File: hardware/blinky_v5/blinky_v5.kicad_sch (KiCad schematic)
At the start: 239 parts, among them J1 RJ45, J10 Conn_01x04, J11 Conn_01x08, J12 Conn_01x06, J2 Conn_01x06_Pin, J3 Conn_01x05_Pin, J5 Conn_01x06_Pin, J6 Conn_01x04_Pin, J7 Conn_01x04_Pin, J8 Conn_01x02, J9 Conn_02x10_Odd_Even, Q1 2N7002, Q10 2N7002, Q2 2N7002, Q3 2N7002, Q4 2N7002, Q5 2N7002, Q6 2N7002, Q7 2N7002, Q8 2N7002, Q9 2N7002, U1 ADA4807-1, U10 STM32F405RGTx, U11 AMS1117-3.3, U12 BA50DD0WHFP-TR, U13 M24C02-RMN, U2 SN74LVC1G14DBV, U3 SN74LVC1G14DBV, U4 ADA4807-1, U5 ADA4807-1, U6 TLV3603DCKR, U7 SN74LVC1G14DBV, U8 TLV3603DCKR, U9 L78L05_SOT89, X1 GTXO-14V (2.048MHz), X2 GTXO-14V (2.048MHz), Y1 AOCJY4A-10.000MHZ-SW, Y2 16MHz

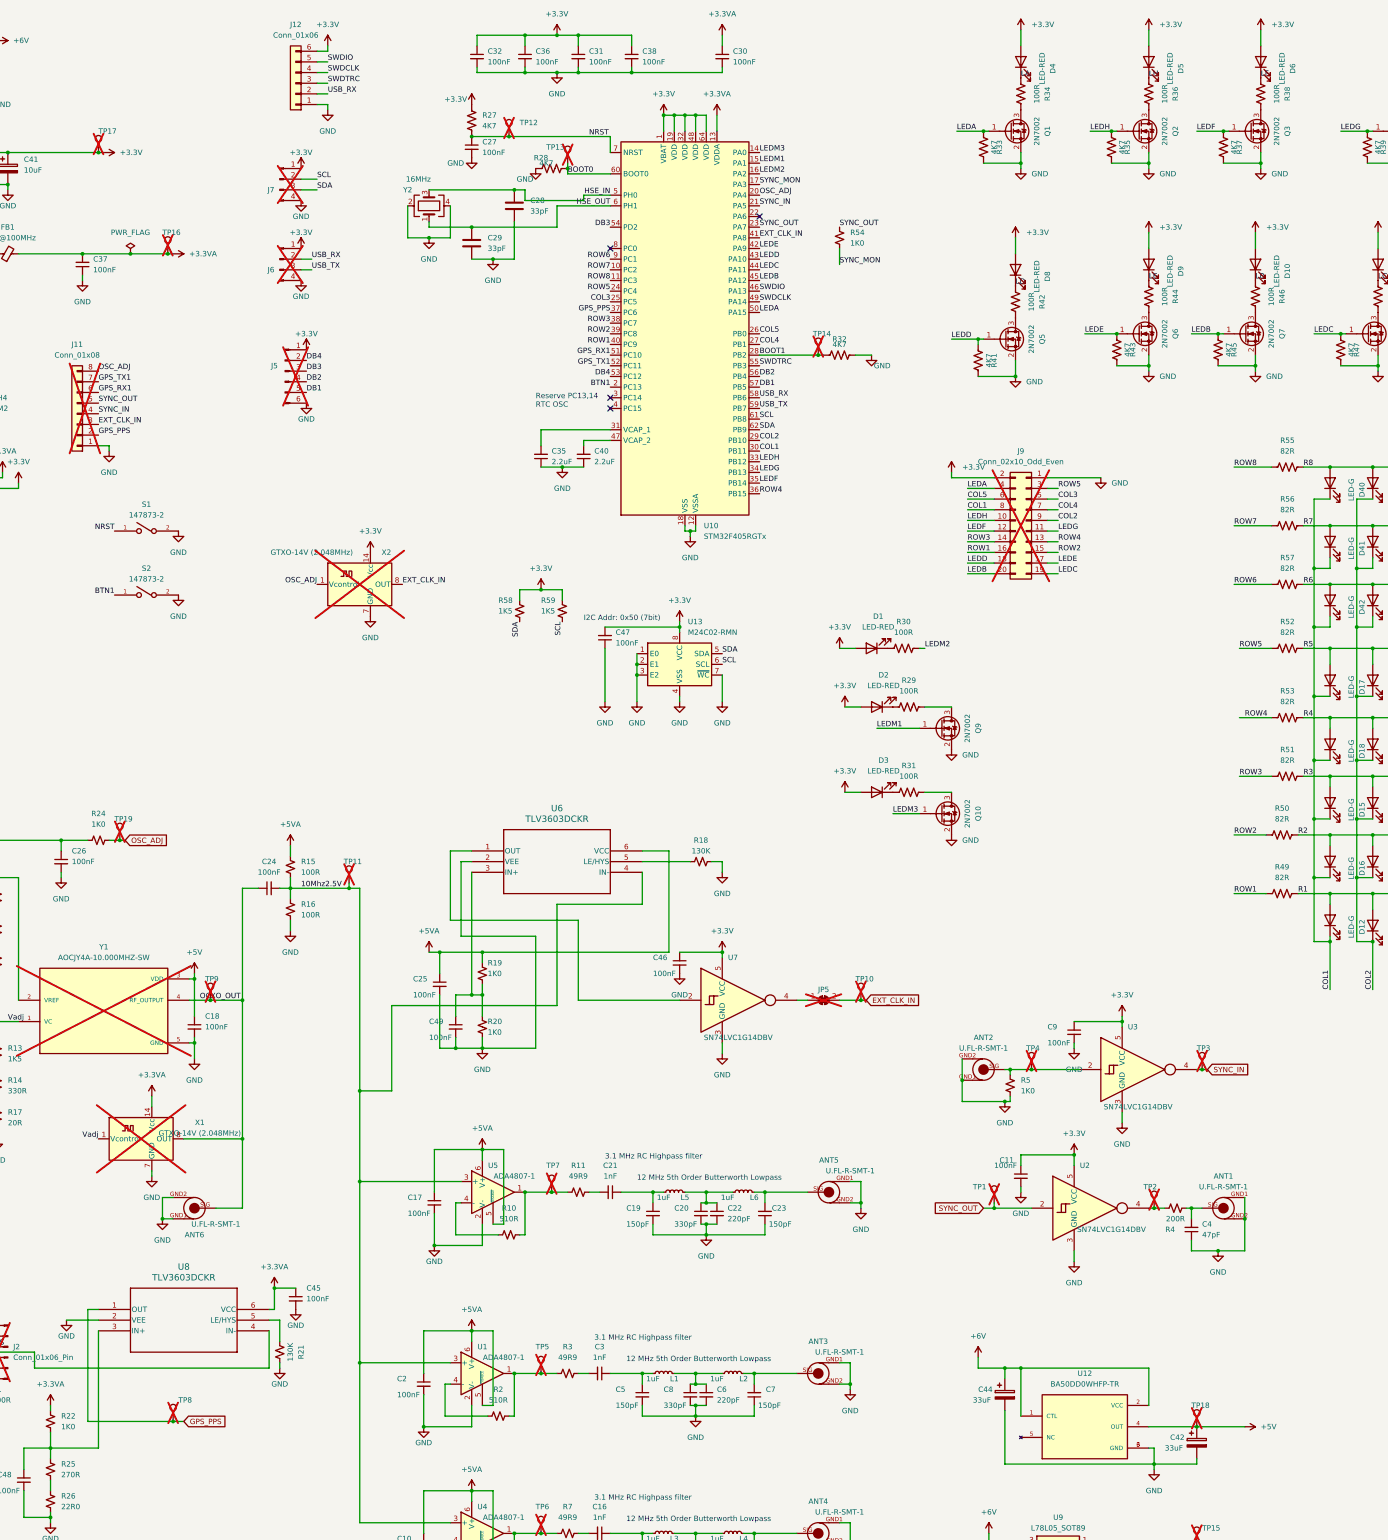
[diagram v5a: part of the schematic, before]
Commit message: update schematic for new pin out
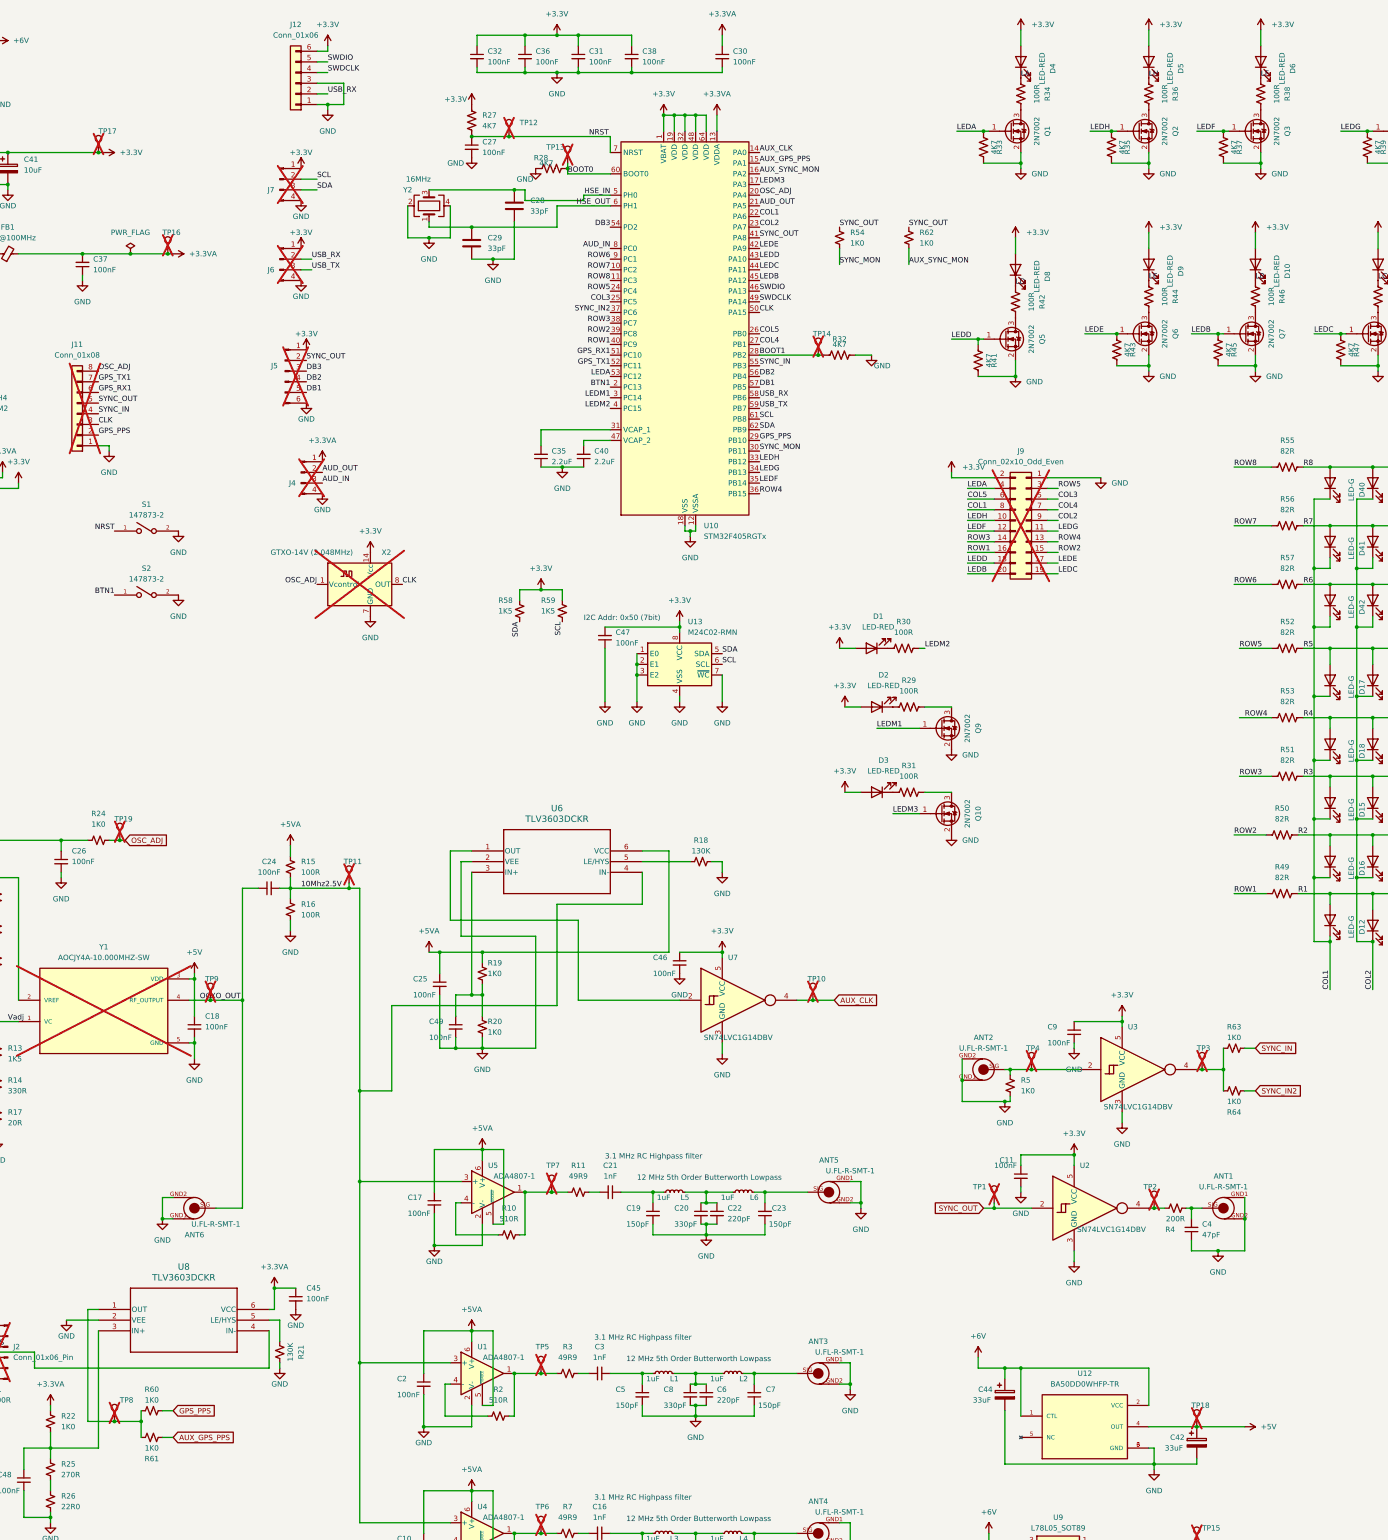
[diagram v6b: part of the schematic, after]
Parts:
- removed JP5: SolderJumper_2_Bridged, Jumper:SolderJumper-2_P1.3mm_Bridged_RoundedPad1.0x1.5mm, symbol Jumper:SolderJumper_2_Bridged
- removed X1: GTXO-14V (2.048MHz), Oscillator:Oscillator_DIP-14, symbol Oscillator:GTXO-14V
- added J4: Conn_01x04_Pin, Connector_PinHeader_2.54mm:PinHeader_1x04_P2.54mm_Vertical, symbol Connector:Conn_01x04_Pin
- added R60, R61, R62, R63, R64: 1K0, Resistor_SMD:R_0603_1608Metric, symbol Device:R_Small_US
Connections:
- net +3.3VA: now also J4.1 (Pin_1)
- net COL1: now also U10.22 (PA6); no longer U10.30 (PB11)
- net COL2: now also U10.23 (PA7); no longer U10.29 (PB10)
- net GND: now also J12.3 (Pin_3), J4.4 (Pin_4)
- net GPS_PPS: now also U10.29 (PB10), R60.1; no longer TP8.1, U10.37 (PC6), U8.1 (OUT)
- net LEDA: now also U10.53 (PC12); no longer U10.50 (PA15)
- net LEDM1: now also U10.3 (PC14); no longer U10.15 (PA1)
- net LEDM2: now also U10.4 (PC15); no longer U10.16 (PA2)
- net LEDM3: now also U10.17 (PA3); no longer U10.14 (PA0)
- net SYNC_IN: now also U10.55 (PB3), R63.1; no longer TP3.1, U10.21 (PA5), U3.4
- net SYNC_MON: now also U10.30 (PB11); no longer U10.17 (PA3)
- net SYNC_OUT: now also J5.2 (Pin_2), U10.41 (PA8), R62.1; no longer U10.23 (PA7)
- net AUX_CLK: now reaches U7.4
- net AUX_CLK: now also TP10.1, U10.14 (PA0)
- net AUD_IN: now reaches U10.8 (PC0)
- net AUD_IN: now also J4.3 (Pin_3)
- removed net DB4: J5.2 (Pin_2), U10.53 (PC12)
- net EXT_CLK_IN renamed CLK
- net CLK: now also U10.50 (PA15); no longer TP10.1, U10.41 (PA8)
- removed net SWDTRC: J12.3 (Pin_3), U10.55 (PB3)
- new net: R60.2, R61.1, TP8.1, U8.1 (OUT)
- new net: R63.2, R64.2, TP3.1, U3.4
- new net AUD_OUT: J4.2 (Pin_2), U10.21 (PA5)
- new net AUX_GPS_PPS: R61.2, U10.15 (PA1)
- new net AUX_SYNC_MON: R62.2, U10.16 (PA2)
- new net SYNC_IN2: R64.1, U10.37 (PC6)
- no-connect marks 4 -> 0
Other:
- note removed: "Reserve PC13,14 RTC OSC"
- moved on the sheet: TP10, TP8

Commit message: update scehmatic with new pin out
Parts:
- removed J10: Conn_01x04, Connector_PinHeader_2.54mm:PinHeader_1x04_P2.54mm_Vertical, symbol Connector_Generic:Conn_01x04
- removed J11: Conn_01x08, Connector_PinHeader_2.54mm:PinHeader_1x08_P2.54mm_Vertical, symbol Connector_Generic:Conn_01x08
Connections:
- net LEDM1: now also U10.4 (PC15); no longer U10.3 (PC14)
- net LEDM2: now also U10.17 (PA3); no longer U10.4 (PC15)
- net LEDM3: now also U10.3 (PC14); no longer U10.17 (PA3)

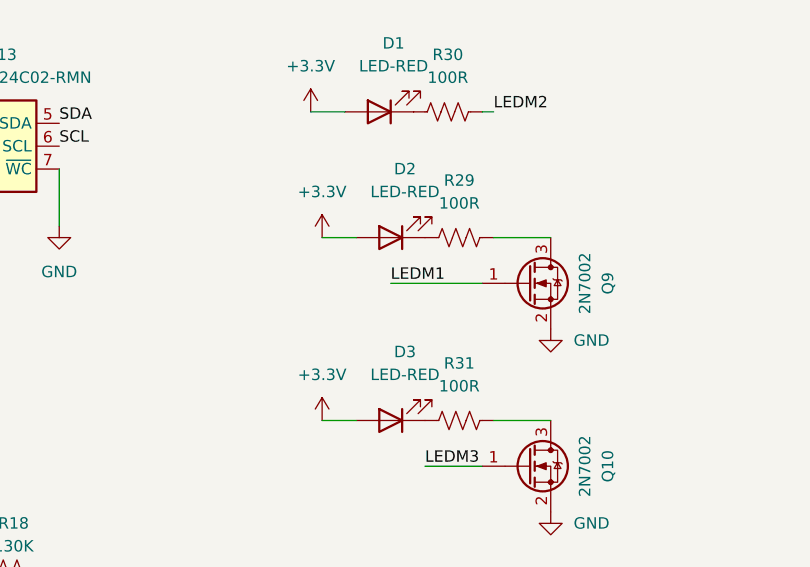
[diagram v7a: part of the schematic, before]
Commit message: change color of status LEDs
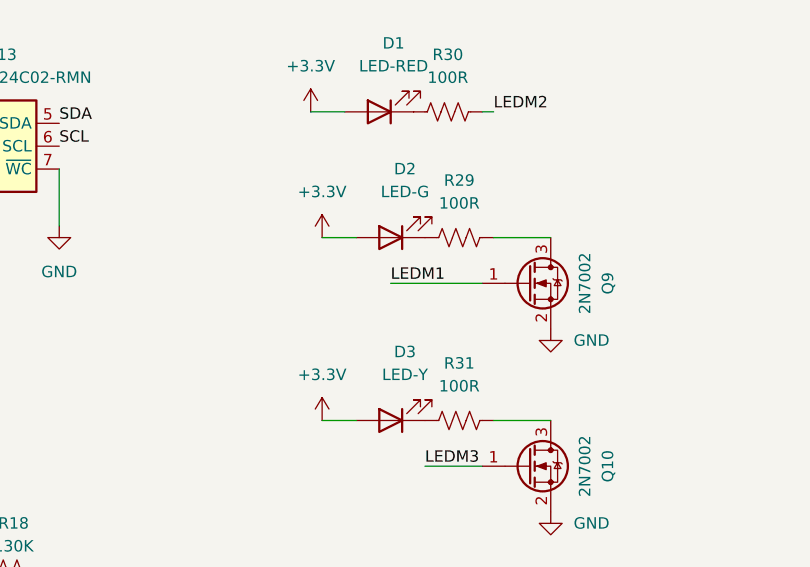
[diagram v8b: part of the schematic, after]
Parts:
- D2: value LED-RED -> LED-G; LCSC C94869 -> C125093
- D3: value LED-RED -> LED-Y; LCSC C94869 -> C72038
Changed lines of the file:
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@@
       (effects (font (size 1.27 1.27)))
     )
-    (property "Value" "LED-RED" (at 256.8575 204.47 0)
+    (property "Value" "LED-Y" (at 256.8575 204.47 0)
       (effects (font (size 1.27 1.27)))
     )
@@
       (effects (font (size 1.27 1.27)) hide)
     )
-    (property "LCSC" "C94869" (at 255.27 209.55 0)
+    (property "LCSC" "C72038" (at 255.27 209.55 0)
       (effects (font (size 1.27 1.27)) hide)
     )
@@
       (effects (font (size 1.27 1.27)))
     )
-    (property "Value" "LED-RED" (at 256.8575 184.15 0)
+    (property "Value" "LED-G" (at 256.8575 184.15 0)
       (effects (font (size 1.27 1.27)))
     )
@@
       (effects (font (size 1.27 1.27)) hide)
     )
-    (property "LCSC" "C94869" (at 255.27 189.23 0)
-      (effects (font (size 1.27 1.27)) hide)
-    )
+    (property "LCSC" "C125093" (at 255.27 189.23 0)
+      (effects (font (size 1.27 1.27)) hide)
+    )
